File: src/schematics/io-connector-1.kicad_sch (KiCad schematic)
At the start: 1 part

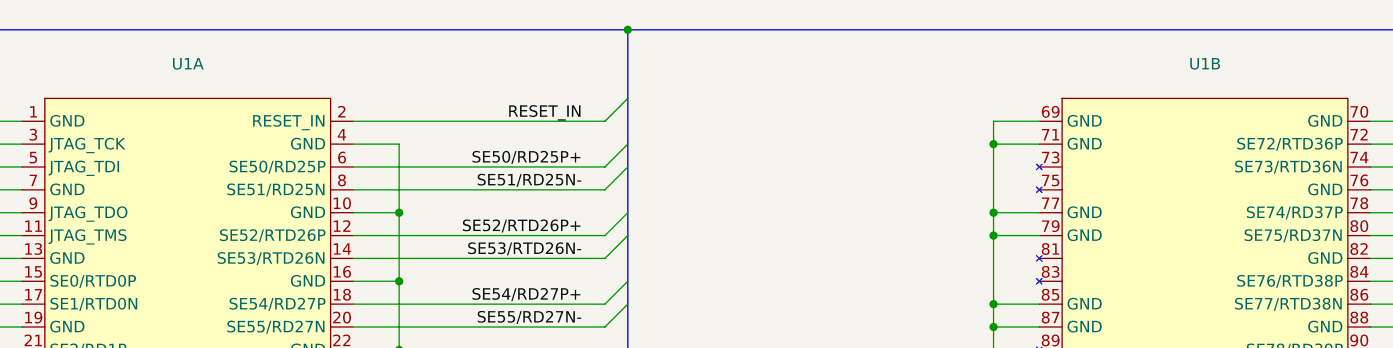
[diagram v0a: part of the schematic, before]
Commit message: Adds the clock oscillator
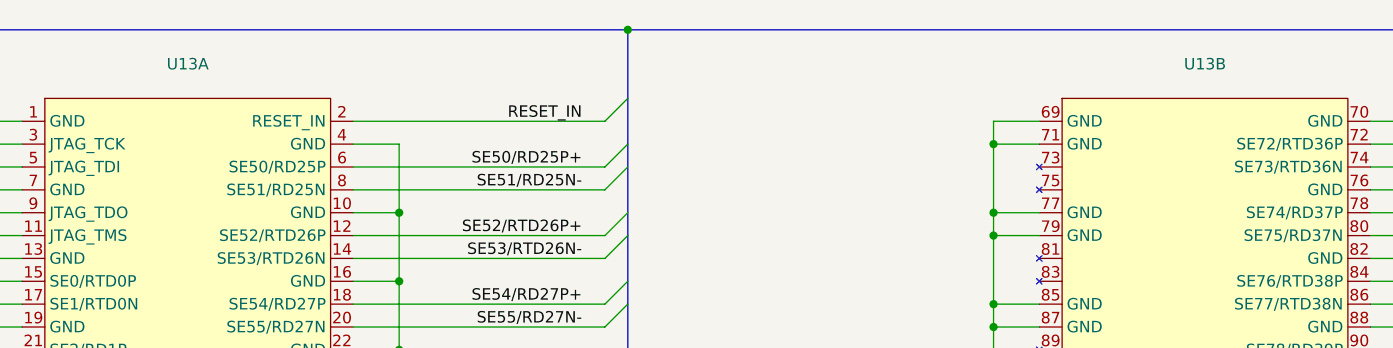
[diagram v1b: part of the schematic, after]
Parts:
- renumbered U1 to U13
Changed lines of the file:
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@@
 		(dnp no)
 		(fields_autoplaced yes)
-		(property "Reference" "#PWR03"
+		(property "Reference" "#PWR0143"
 			(at 115.57 144.78 0)
 			(effects
@@
 			(project "ecap5-bsom"
 				(path "/c5fd18a3-9aa0-4151-b6e0-94da3d606686/25311f3d-42bc-4bc6-b069-9a914cc16127/9b7e9ac9-0b74-4ac0-9962-3e0d280c31a1"
-					(reference "#PWR03")
+					(reference "#PWR0143")
 					(unit 1)
 				)
@@
 		(dnp no)
 		(fields_autoplaced yes)
-		(property "Reference" "#PWR026"
+		(property "Reference" "#PWR0145"
 			(at 228.6 144.78 0)
 			(effects
@@
 			(project "ecap5-bsom"
 				(path "/c5fd18a3-9aa0-4151-b6e0-94da3d606686/25311f3d-42bc-4bc6-b069-9a914cc16127/9b7e9ac9-0b74-4ac0-9962-3e0d280c31a1"
-					(reference "#PWR026")
+					(reference "#PWR0145")
 					(unit 1)
 				)
@@
 		(dnp no)
 		(fields_autoplaced yes)
-		(property "Reference" "#PWR02"
+		(property "Reference" "#PWR0142"
 			(at 68.58 144.78 0)
 			(effects
@@
 			(project "ecap5-bsom"
 				(path "/c5fd18a3-9aa0-4151-b6e0-94da3d606686/25311f3d-42bc-4bc6-b069-9a914cc16127/9b7e9ac9-0b74-4ac0-9962-3e0d280c31a1"
-					(reference "#PWR02")
+					(reference "#PWR0142")
 					(unit 1)
 				)
@@
 		(dnp no)
 		(fields_autoplaced yes)
-		(property "Reference" "U1"
+		(property "Reference" "U13"
 			(at 205.105 44.45 0)
 			(effects
@@
 			(project "ecap5-bsom"
 				(path "/c5fd18a3-9aa0-4151-b6e0-94da3d606686/25311f3d-42bc-4bc6-b069-9a914cc16127/9b7e9ac9-0b74-4ac0-9962-3e0d280c31a1"
-					(reference "U1")
+					(reference "U13")
 					(unit 2)
 				)
@@
 	)
 	(symbol
-		(lib_name "IO_CONN_1")
 		(lib_id "ECAP5-BSOM:IO_CONN")
 		(at 92.71 92.71 0)
@@
 		(dnp no)
 		(fields_autoplaced yes)
-		(property "Reference" "U1"
+		(property "Reference" "U13"
 			(at 92.075 44.45 0)
 			(effects
@@
 			(project "ecap5-bsom"
 				(path "/c5fd18a3-9aa0-4151-b6e0-94da3d606686/25311f3d-42bc-4bc6-b069-9a914cc16127/9b7e9ac9-0b74-4ac0-9962-3e0d280c31a1"
-					(reference "U1")
+					(reference "U13")
 					(unit 1)
 				)
@@
 		(dnp no)
 		(fields_autoplaced yes)
-		(property "Reference" "#PWR05"
+		(property "Reference" "#PWR0144"
 			(at 181.61 144.78 0)
 			(effects
@@
 			(project "ecap5-bsom"
 				(path "/c5fd18a3-9aa0-4151-b6e0-94da3d606686/25311f3d-42bc-4bc6-b069-9a914cc16127/9b7e9ac9-0b74-4ac0-9962-3e0d280c31a1"
-					(reference "#PWR05")
+					(reference "#PWR0144")
 					(unit 1)
 				)

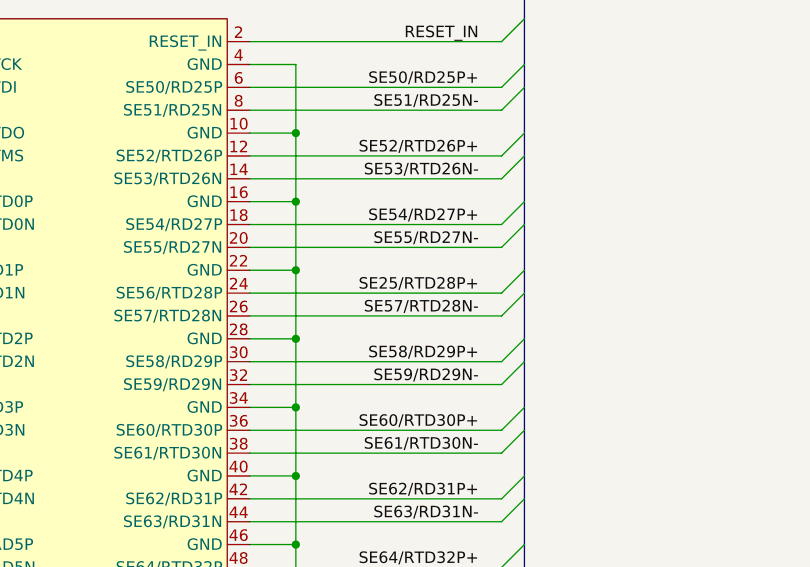
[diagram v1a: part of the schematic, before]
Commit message: Adds bus aliases
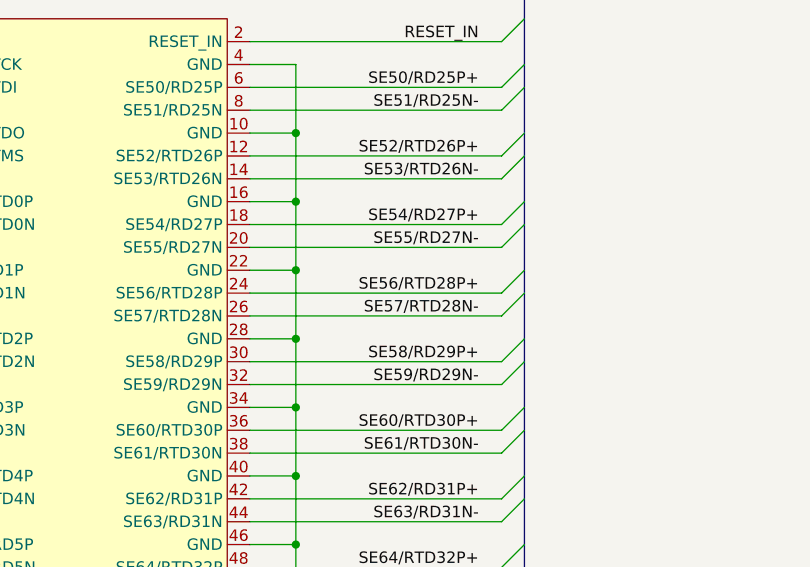
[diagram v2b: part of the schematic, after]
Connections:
- net SE25/RTD28P+ renamed SE56/RTD28P+
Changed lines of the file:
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@@
 		(rev "${Revision}")
 		(comment 1 "${Project Title}")
-		(comment 2 "IO CONNECTOR")
+		(comment 2 "IO CONNECTOR 1")
 		(comment 3 "${Part Number}")
 	)
+	(bus_alias "IO"
+		(members "JTAG_TCK" "JTAG_TDI" "JTAG_TDO" "JTAG_TMS" "SE0/RTD0P+" "SE1/RTD0N-"
+			"SE2/RD1P+" "SE3/RD1N-" "SE4/RTD2P+" "SE5/RTD2N-" "SE6/RD3P+" "SE7/RD3N-"
+			"SE8/RTD4P+" "SE9/RTD4N-" "SE10/RD5P+" "SE11/RD5N-" "SE12/RTD6P+" "SE13/RTD6N-"
+			"SE14/RD7P+" "SE15/RD7N-" "RESET_IN" "SE50/RD25P+" "SE51/RD25N-" "SE52/RTD26P+"
+			"SE53/RTD26N-" "SE54/RD27P+" "SE55/RD27N-" "SE56/RTD28P+" "SE57/RTD28N-"
+			"SE58/RD29P+" "SE59/RD29n-" "SE60/RTD30P+" "SE61/RTD30N-" "SE62/RD31P+"
+			"SE63/RD31N-" "SE64/RTD32P+" "SE65/RTD32N-" "SE66/RD33P+" "SE67/RD33N-"
+			"SE68/RTD34P+" "SE69/RTD34N-" "SE70/RD35P+" "SE71/RD35N-" "SE72/RTD36P+"
+			"SE73/RTD36N-" "SE74/RD37P+" "SE75/RD37N-" "SE76/RTD38P+" "SE77/RTD38N-"
+			"SE78/RD39P+" "SE79/RD39N-" "SE80/RTD40P+" "SE81/RTD40N-" "SE82/RD41P+"
+			"SE83/RD41N-" "SE84/RTD42P+" "SE85/RTD42N-" "SE86/RD43P+" "SE87/RD43N-"
+			"SE88/RTD44P+" "SE89/RTD44N-" "SE90/RD45P+" "SE91/RD45N-" "SE92/RTD46P+"
+			"SE93/RTD46N-" "SE131" "SE16/RTD8P+" "SE17/RTD8N-" "SE18/RD9P+" "SE19/RD9N-"
+			"SE20/RTD10P+" "SE21/RTD10N-" "SE22/RD11P+" "SE23/RD11N-" "SE24/RTD12P+"
+			"SE25/RTD12N-" "SE26/RD13P+" "SE27/RD13N-" "SE28/RTD14P+" "SE29/RTD14N-"
+			"SE30/RD15P+" "SE31/RD12N-" "SE94/RD47P+" "SE95/RD47N-" "SE96/RTD48P+"
+			"SE97/RTD48N-" "SE98/RD49P+" "SE99/RD49N-" "SE100/RTD50P+" "SE101/RTD50N-"
+			"SE102/RD51P+" "SE103/RD51N-" "SE104/RTD52P+" "SE105/RTD52N-" "SE106/RD53P+"
+			"SE107/RD53N-" "SE108/RTD54P+" "SE109/RTD54N-" "SE110/RD55P+" "SE111/RD55N-"
+			"SE32/RTD16P+" "SE33/RTD16N-" "SE34/RD17P+" "SE35/RD17N-" "SE36/RTD18P+"
+			"SE37/RTD18N-" "SE38/RD19P+" "SE39/RD19N-" "SE40/RTD20P+" "SE41/RTD20N-"
+			"SE42/RD21P+" "SE43/RD21N-" "SE44/RTD22P+" "SE45/RTD22N-" "SE46/RD23P+"
+			"SE47/RD23N-" "SE48/RTD24P+" "SE49/RTD24N-" "SE112/RTD56P+" "SE113/RTD56N-"
+			"SE114/RD57P+" "SE115/RD57N-" "SE116/RTD58P+" "SE117/RTD58N-" "SE118/RD59P+"
+			"SE119/RD59N-" "SE120/RTD60P+" "SE121/RTD60N-" "SE122/RD61P+" "SE123/RD61N-"
+			"SE124/RTD62P+" "SE125/RTD62N-" "SE126/RD63P+" "SE127/RD63N-" "SE128/RTD64P+"
+			"SE129/RTD64N-" "SE130"
+		)
+	)
 	(junction
 		(at 115.57 121.92)
@@
 		)
 	)
-	(label "SE25{slash}RTD28P+"
+	(label "SE56{slash}RTD28P+"
 		(at 135.89 78.74 180)
 		(fields_autoplaced yes)

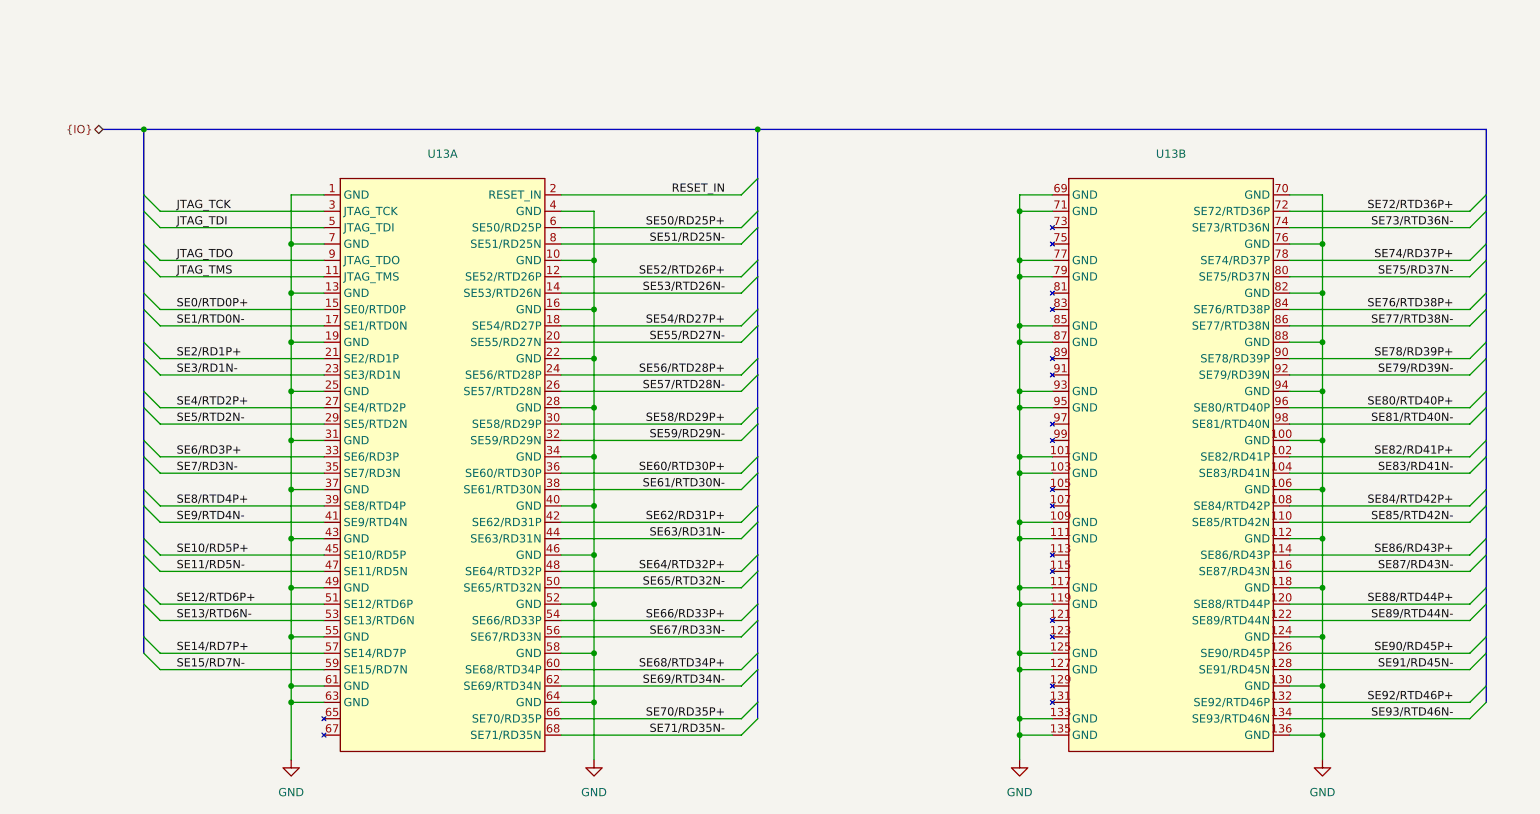
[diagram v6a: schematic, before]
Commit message: ✨ Add net classes to the schematic (#38)
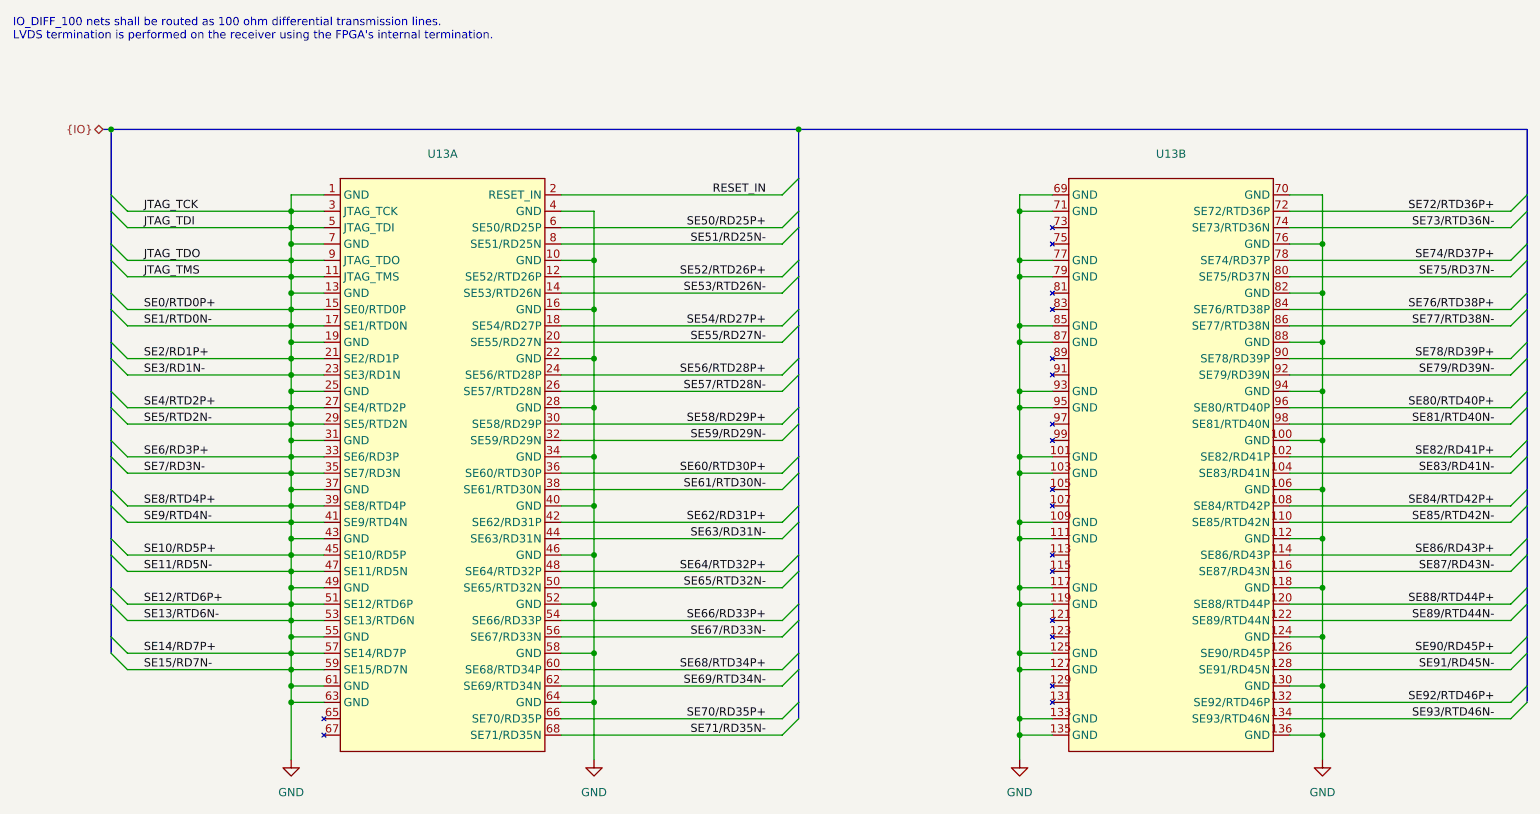
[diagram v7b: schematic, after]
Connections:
- net JTAG_TCK is gone; now on net GND: U13.3 (JTAG_TCK)
- net JTAG_TDI is gone; now on net GND: U13.5 (JTAG_TDI)
- net JTAG_TDO is gone; now on net GND: U13.9 (JTAG_TDO)
- net JTAG_TMS is gone; now on net GND: U13.11 (JTAG_TMS)
- net SE0/RTD0P+ is gone; now on net GND: U13.15 (SE0/RTD0P)
- net SE10/RD5P+ is gone; now on net GND: U13.45 (SE10/RD5P)
- net SE11/RD5N- is gone; now on net GND: U13.47 (SE11/RD5N)
- net SE12/RTD6P+ is gone; now on net GND: U13.51 (SE12/RTD6P)
- net SE13/RTD6N- is gone; now on net GND: U13.53 (SE13/RTD6N)
- net SE14/RD7P+ is gone; now on net GND: U13.57 (SE14/RD7P)
- net SE15/RD7N- is gone; now on net GND: U13.59 (SE15/RD7N)
- net SE1/RTD0N- is gone; now on net GND: U13.17 (SE1/RTD0N)
- net SE2/RD1P+ is gone; now on net GND: U13.21 (SE2/RD1P)
- net SE3/RD1N- is gone; now on net GND: U13.23 (SE3/RD1N)
- net SE4/RTD2P+ is gone; now on net GND: U13.27 (SE4/RTD2P)
- net SE5/RTD2N- is gone; now on net GND: U13.29 (SE5/RTD2N)
- net SE6/RD3P+ is gone; now on net GND: U13.33 (SE6/RD3P)
- net SE7/RD3N- is gone; now on net GND: U13.35 (SE7/RD3N)
- net SE8/RTD4P+ is gone; now on net GND: U13.39 (SE8/RTD4P)
- net SE9/RTD4N- is gone; now on net GND: U13.41 (SE9/RTD4N)
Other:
- note added: "IO_DIFF_100 nets shall be routed as 100 ohm differential transmission lines. LVDS termination is performed on the receiver using the FPGA's internal termination."
